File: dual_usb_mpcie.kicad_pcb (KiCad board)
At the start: 2 copper layers, 73.7 x 91.6 mm, 28 parts, among them J1 91304-56-052R2, J2 91304-56-052R2, J3 USB, U1 AZ1117H-3.3, U2 AZ1117H-3.3, U3 AZ1117H-1.5, U4 AZ1117H-1.5

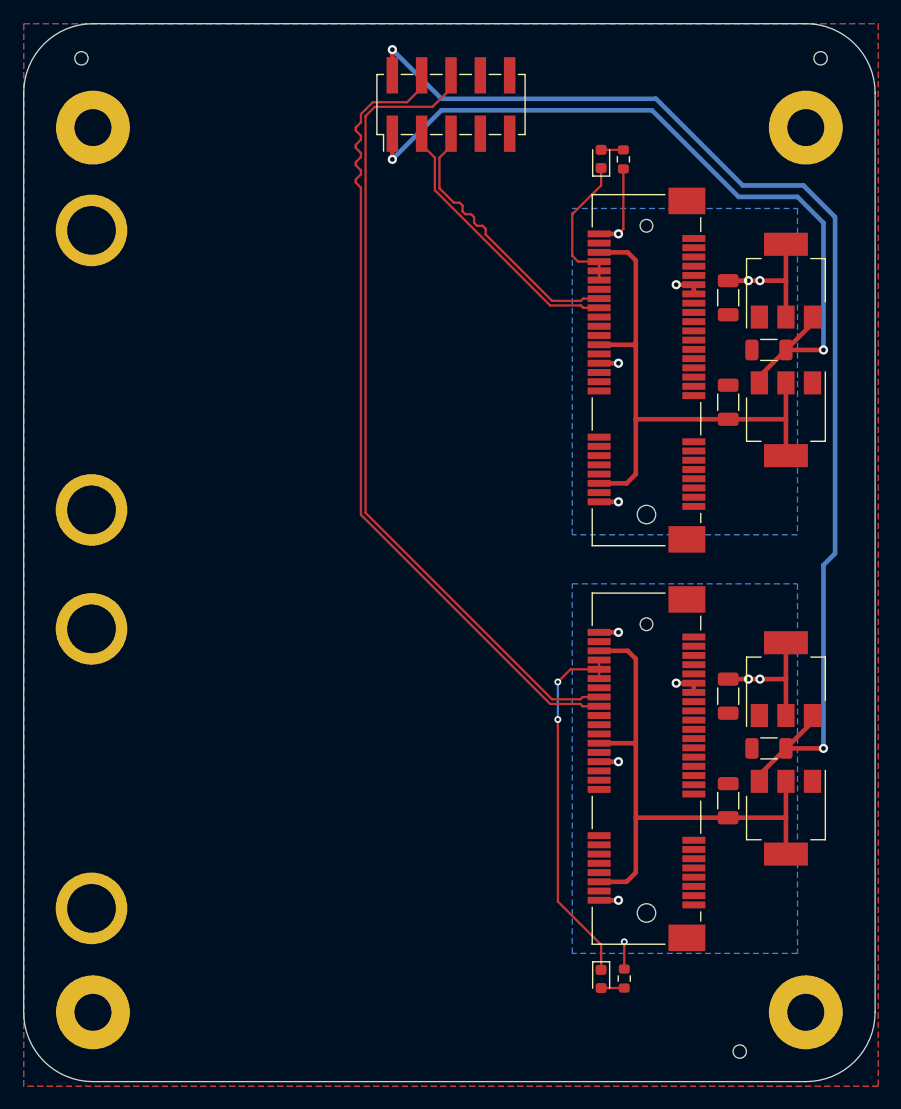
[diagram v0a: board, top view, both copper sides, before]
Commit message: Remove 1.5v. Change bottom pour to shield. Couple shield with ground. Add pull-up to W_DIS and PCIE_RST.
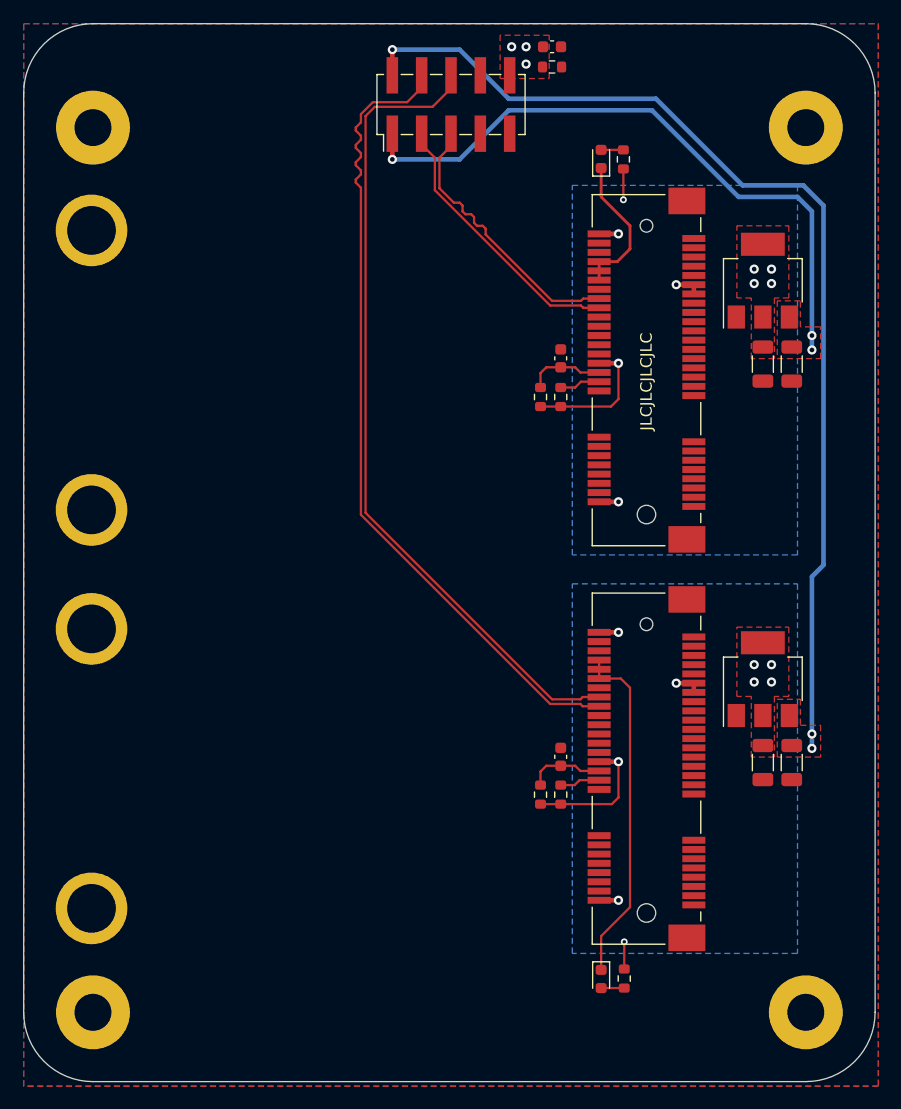
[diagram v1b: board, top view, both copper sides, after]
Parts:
- removed FID1, FID2, FID3: Fiducial, parts:fiducial_jlcpcb_smt
- removed U3, U4: AZ1117H-1.5, Package_TO_SOT_SMD:SOT-223-3_TabPin2
- added C7: 0.1uF, Capacitor_SMD:C_0603_1608Metric, F.Cu at (99.8, 53.0)
- added R3: 1M, Resistor_SMD:R_0603_1608Metric, F.Cu at (99.8, 54.8)
- added R4: 3.3k, Resistor_SMD:R_0603_1608Metric, F.Cu at (100.5, 117.8)
- added R5: 3.3k, Resistor_SMD:R_0603_1608Metric, F.Cu at (98.8, 117.8)
- added R6: 3.3k, Resistor_SMD:R_0603_1608Metric, F.Cu at (100.5, 83.3)
- added R7: 3.3k, Resistor_SMD:R_0603_1608Metric, F.Cu at (98.8, 83.3)
- C5, C6: value 22uF -> 0.1uF; footprint Capacitor_SMD:C_1206_3216Metric -> Capacitor_SMD:C_0603_1608Metric
- moved C6 41.0 mm to (100.5, 80.0)
- moved C5 34.0 mm to (100.5, 114.5)
- moved C1 6.49 mm to (118.0, 80.5)
- moved C3 6.49 mm to (118.0, 115.0)
- moved C2 2.32 mm to (120.5, 80.5), turned to -90 degrees
- moved C4 2.32 mm to (120.5, 115.0), turned to -90 degrees
- moved U1 2.00 mm to (118.0, 73.2)
- moved U2 2.00 mm to (118.0, 107.8)
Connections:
- C5 pad 1: +1.5V_A -> Net-(J2-~{PERST})
- C6 pad 1: +1.5V_B -> Net-(J1-~{PERST})
- H1 pad 1: GND -> /SHIELD
- H2 pad 1: GND -> /SHIELD
- H3 pad 1: GND -> /SHIELD
- H4 pad 1: GND -> /SHIELD
- J1 pad 20: unconnected-(J1-~{W_DISABLE}-Pad20) -> Net-(J1-~{W_DISABLE})
- J1 pad 22: unconnected-(J1-~{PERST}-Pad22) -> Net-(J1-~{PERST})
- J1 pad 28: +1.5V_A -> unconnected-(J1-+1V5-Pad28)
- J1 pad 48: +1.5V_A -> unconnected-(J1-+1V5-Pad48)
- J1 pad 6: +1.5V_A -> unconnected-(J1-+1V5-Pad6)
- J2 pad 20: unconnected-(J2-~{W_DISABLE}-Pad20) -> Net-(J2-~{W_DISABLE})
- J2 pad 22: unconnected-(J2-~{PERST}-Pad22) -> Net-(J2-~{PERST})
- J2 pad 28: +1.5V_B -> unconnected-(J2-+1V5-Pad28)
- J2 pad 48: +1.5V_B -> unconnected-(J2-+1V5-Pad48)
- J2 pad 6: +1.5V_B -> unconnected-(J2-+1V5-Pad6)
- J3 pad 10: unconnected-(J3-Pin_10-Pad10) -> /SHIELD
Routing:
- net +1.5V_B: track 47.9 -> 0.00 mm
- net +1.5V_A: track 47.9 -> 0.00 mm
- net +5V_B: track 103.8 -> 92.6 mm, vias 2 -> 3
- net +5V_A: track 67.2 -> 55.9 mm, vias 2 -> 3
- net Net-(J1-~{PERST}): track 0.00 -> 6.72 mm
- net Net-(J2-~{PERST}): track 0.00 -> 6.64 mm
- net +3.3V_A: track 24.5 -> 20.1 mm, vias 6 -> 9
- net Net-(J1-~{W_DISABLE}): track 0.00 -> 3.53 mm
- net Net-(J2-~{W_DISABLE}): track 0.00 -> 3.50 mm
- net Net-(D2-K): track 32.1 -> 30.1 mm, vias 2 -> 0
- net +3.3V_B: track 21.0 -> 19.8 mm, vias 7 -> 9
- net /SHIELD: vias 0 -> 3
- added copper zone on F.Cu, net +3.3V_A
- added copper zone on F.Cu, net +3.3V_B
- added copper zone on F.Cu, net +5V_A
- added copper zone on F.Cu, net +5V_B
- added copper zone on B.Cu, net /SHIELD
- added copper zone on F.Cu, net /SHIELD
- removed copper zone on B.Cu, net GND

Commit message: Rotate mpcie connectors so all routing is at the top of the board. Move power to the top. Move up mpcie connectors. Add silkscreen. Add models to mpcie and standoff
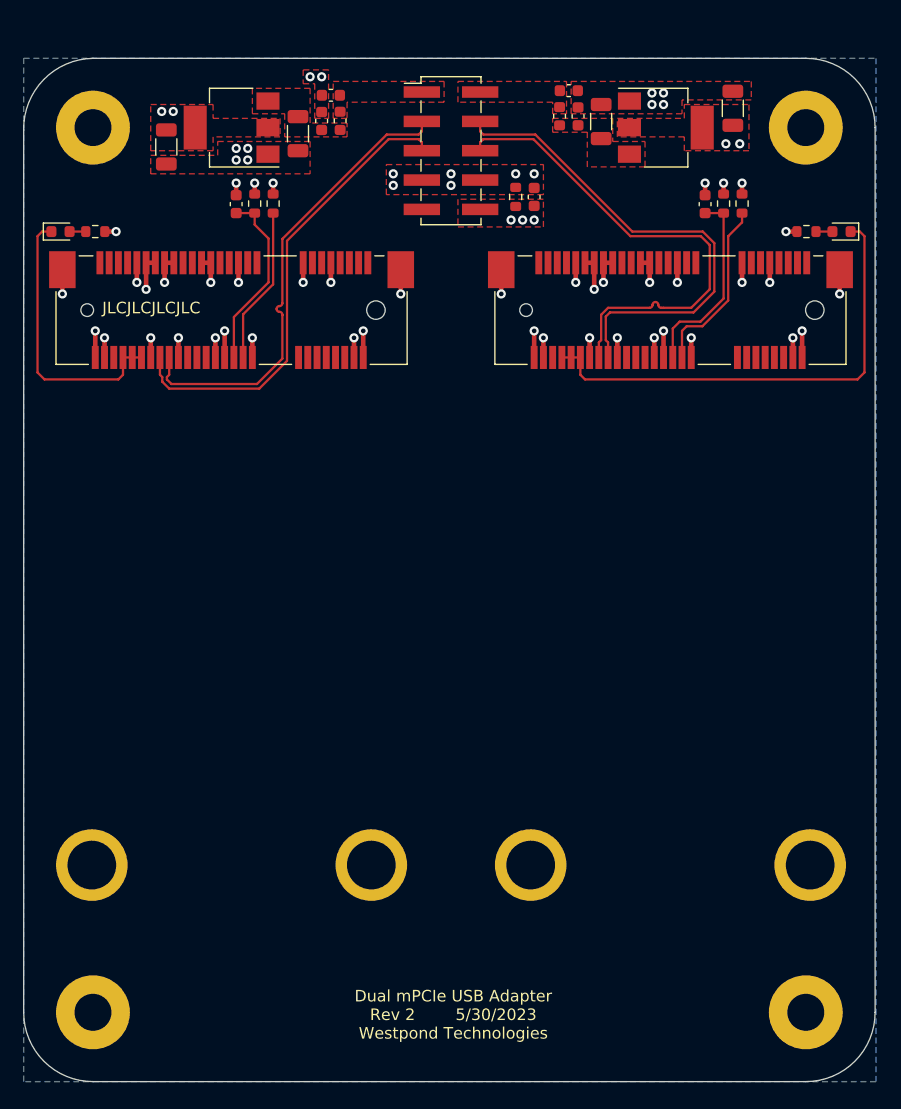
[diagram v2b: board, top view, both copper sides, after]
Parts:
- added C10: 0.01uF, Capacitor_SMD:C_0603_1608Metric, F.Cu at (80.6, 57.2)
- added C11: 0.01uF, Capacitor_SMD:C_0603_1608Metric, F.Cu at (79.8, 59.4)
- added C8: 0.01uF, Capacitor_SMD:C_0603_1608Metric, F.Cu at (101.2, 56.8)
- added C9: 0.01uF, Capacitor_SMD:C_0603_1608Metric, F.Cu at (102.0, 59.0)
- added FB1: FerriteBead_Small, Inductor_SMD:L_0603_1608Metric, F.Cu at (100.4, 59.0)
- added FB2: FerriteBead_Small, Inductor_SMD:L_0603_1608Metric, F.Cu at (81.4, 59.4)
- C5, C6: value 0.1uF -> 1uF
- moved D2 68.0 mm to (124.8, 69.0), turned to 180 degrees
- moved R2 66.6 mm to (121.8, 69.0), turned to 0 degrees
- moved H8 62.3 mm to (122.1, 123.8), turned to 90 degrees
- moved C4 57.9 mm to (104.0, 59.5), turned to 90 degrees
- moved C3 56.7 mm to (115.4, 58.3), turned to 90 degrees
- moved C1 55.0 mm to (66.3, 61.7)
- moved H5 55.0 mm to (59.9, 123.8), turned to 90 degrees
- moved R5 53.6 mm to (114.6, 66.6), turned to -90 degrees
- moved R4 53.5 mm to (116.2, 66.6), turned to -90 degrees
- moved C5 49.5 mm to (113.0, 66.6)
- moved U2 48.5 mm to (109.6, 60.0), turned to 0 degrees
- moved U1 47.9 mm to (72.0, 60.0), turned to 180 degrees
- moved D1 47.2 mm to (57.2, 69.0), turned to 0 degrees
- moved C2 47.2 mm to (77.8, 60.5)
- moved R1 46.2 mm to (60.2, 69.0), turned to 180 degrees
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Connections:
- J3 pad 1: +5V_A -> /VBUS_A
- J3 pad 2: +5V_B -> /VBUS_B
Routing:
- net +5V_B: track 92.6 -> 0.00 mm, vias 3 -> 0
- net +5V_A: track 55.9 -> 0.00 mm, vias 3 -> 0
- net GND: track 0.00 -> 54.5 mm, vias 0 -> 46
- net /USB_B+: track 70.9 -> 43.0 mm
- net /USB_B-: track 70.9 -> 43.3 mm
- net /USB_A-: track 23.8 -> 40.8 mm
- net /USB_A+: track 24.0 -> 40.8 mm
- net Net-(J2-~{W_DISABLE}): track 3.50 -> 15.5 mm
- net Net-(D1-K): track 12.8 -> 24.1 mm
- net Net-(D2-K): track 30.1 -> 41.3 mm
- net Net-(J2-~{PERST}): track 6.64 -> 17.0 mm
- net Net-(J1-~{W_DISABLE}): track 3.53 -> 13.6 mm
- net Net-(J1-~{PERST}): track 6.72 -> 15.8 mm
- net +3.3V_A: track 20.1 -> 12.9 mm
- net +3.3V_B: track 19.8 -> 12.9 mm
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- added copper zone on In2.Cu, net +3.3V_A
- added copper zone on In2.Cu, net +3.3V_B
- added copper zone on F.Cu, net /VBUS_A
- added copper zone on F.Cu, net /VBUS_B
- added copper zone on In1.Cu, net GND
- removed copper zone on B.Cu, net +3.3V_A
- removed copper zone on B.Cu, net +3.3V_B
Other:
- board size 73.7 x 91.6 mm -> 73.7 x 88.6 mm
- copper layers 2 -> 4
- board text added: "Dual mPCIe USB Adapter Rev 2 5/30/2023 Westpond Technologies"

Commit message: WPE logo
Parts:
- added G***: LOGO, parts:wpe_logo, F.Cu at (90.2, 136.6)
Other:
- board text added: "5/30/2023 R2"
- board text removed: "Dual mPCIe USB Adapter Rev 2 5/30/2023 Westpond Technologies"

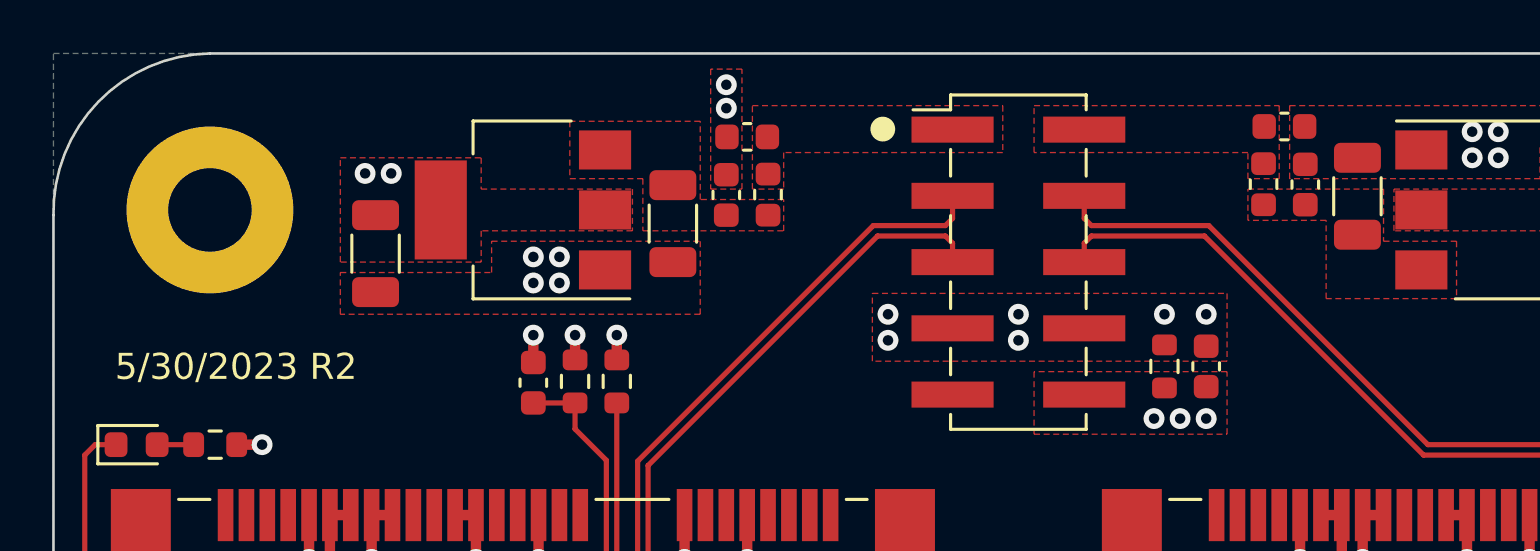
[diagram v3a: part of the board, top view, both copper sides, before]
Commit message: Fix FB size for part. 0603 -> 0805
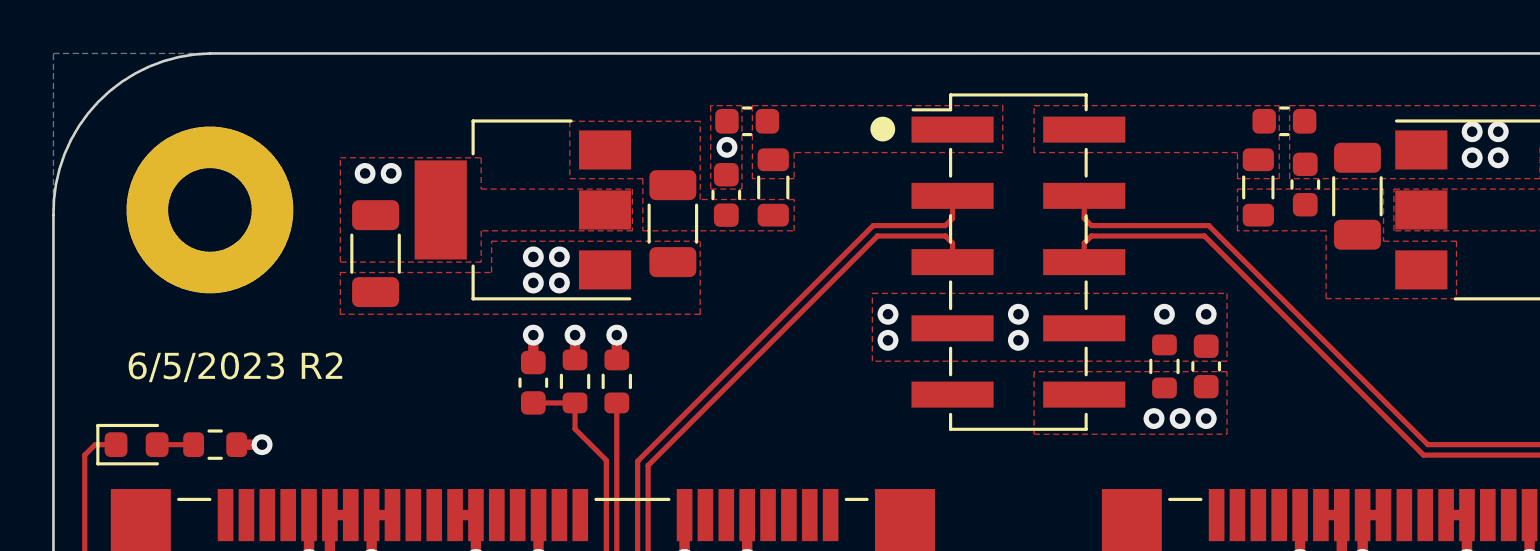
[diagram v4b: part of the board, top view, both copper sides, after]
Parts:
- FB1, FB2: footprint Inductor_SMD:L_0603_1608Metric -> Inductor_SMD:L_0805_2012Metric
- moved C10 0.60 mm to (80.6, 56.6)
- moved FB2 0.34 mm to (81.6, 59.1)
- moved FB1 0.24 mm to (100.2, 59.1)
- moved C8 0.20 mm to (101.2, 56.6)
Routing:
- net GND: vias 46 -> 45
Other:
- board text added: "6/5/2023 R2"
- board text removed: "5/30/2023 R2"
